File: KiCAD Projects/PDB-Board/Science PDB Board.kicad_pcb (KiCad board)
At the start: 2 copper layers, 85.1 x 63.5 mm, 12 parts, among them P1 MOTOR_PWR_OUT, P2 MAIN_PWR_IN, P3 5V_OUT, P4 PWR_REG

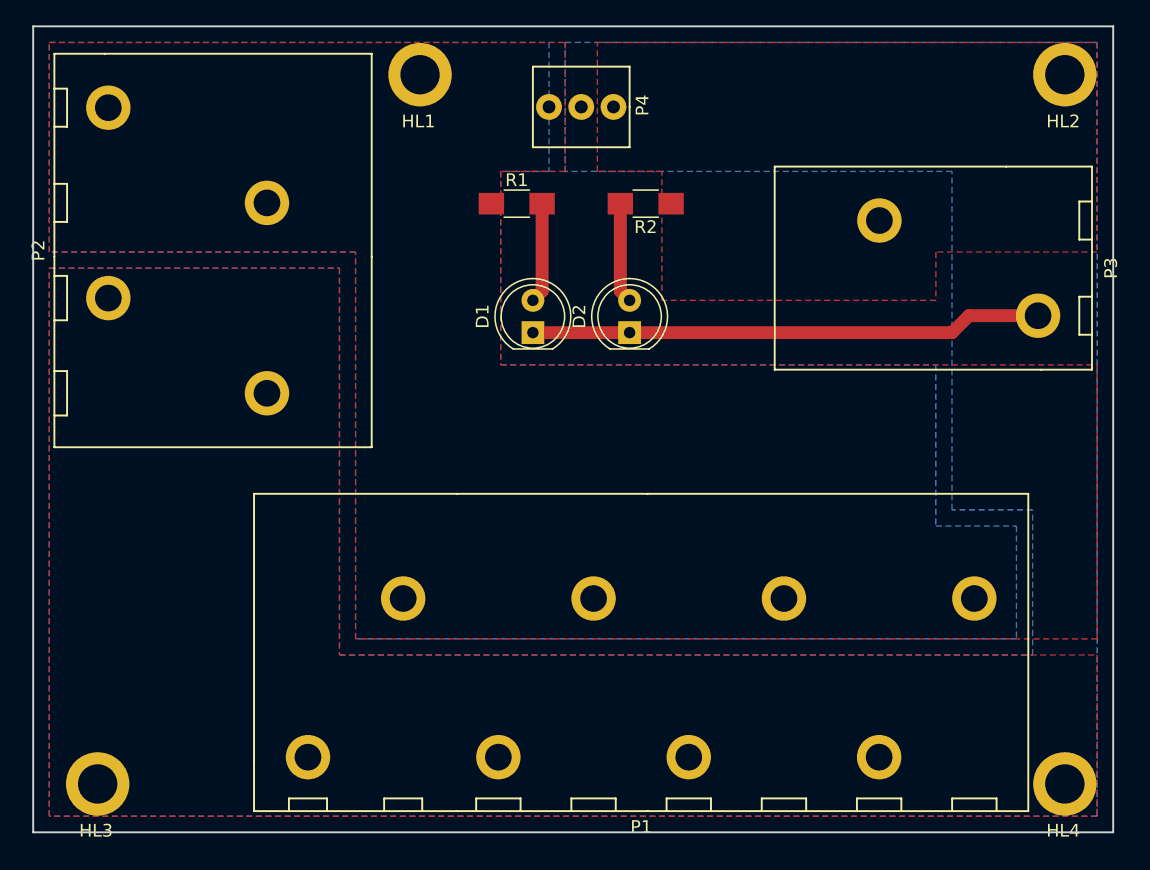
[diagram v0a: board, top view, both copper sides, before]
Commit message: Finished PDB. Actually.
Sending for review.
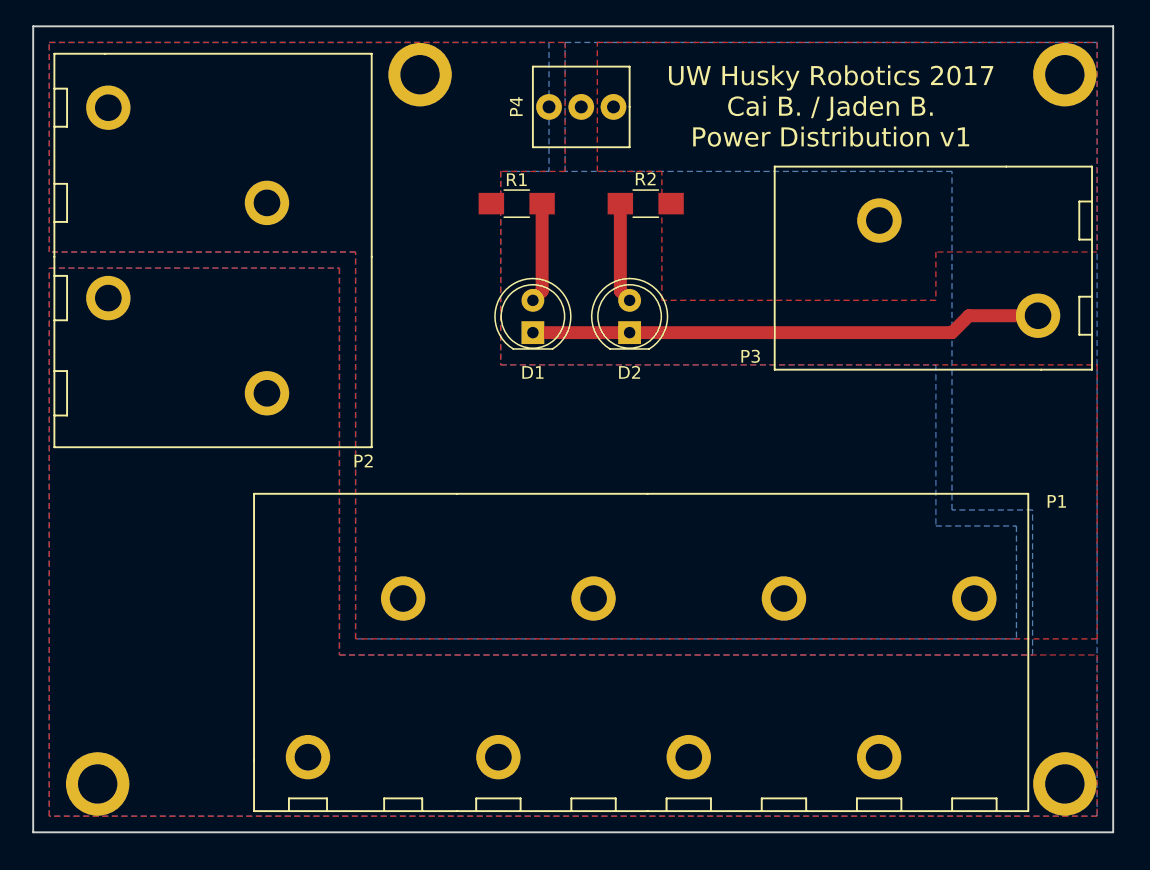
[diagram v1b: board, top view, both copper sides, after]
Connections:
- HL1 pad 1: GND -> Net-(HL1-Pad1)
- HL2 pad 1: GND -> Net-(HL2-Pad1)
- HL3 pad 1: GND -> Net-(HL3-Pad1)
- HL4 pad 1: GND -> Net-(HL4-Pad1)
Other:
- board text added: "UW Husky Robotics 2017 Cai B. / Jaden B. Power Distribution v1"
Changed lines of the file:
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@@
 (kicad_pcb (version 4) (host pcbnew 4.0.3-stable)
   (general
-    (links 24)
-    (no_connects 1)
+    (links 20)
+    (no_connects 0)
     (area 114.224999 76.124999 199.465001 139.775001)
     (thickness 1.6)
-    (drawings 4)
+    (drawings 5)
     (tracks 8)
     (zones 0)
     (modules 12)
-    (nets 6)
+    (nets 10)
   )
   (page A4)
@@
   (net 4 "Net-(D2-Pad2)")
   (net 5 GND)
+  (net 6 "Net-(HL1-Pad1)")
+  (net 7 "Net-(HL2-Pad1)")
+  (net 8 "Net-(HL3-Pad1)")
+  (net 9 "Net-(HL4-Pad1)")
   (net_class Default "This is the default net class."
     (clearance 0.2)
@@
     (add_net "Net-(D1-Pad2)")
     (add_net "Net-(D2-Pad2)")
+    (add_net "Net-(HL1-Pad1)")
+    (add_net "Net-(HL2-Pad1)")
+    (add_net "Net-(HL3-Pad1)")
+    (add_net "Net-(HL4-Pad1)")
   )
   (module Resistors_SMD:R_1206_HandSoldering (layer F.Cu)
@@
       (effects (font (size 1 1) (thickness 0.15)))
     )
-    (fp_text value R (at 0 1.9) (layer F.Fab)
+    (fp_text value R (at 0 0) (layer F.Fab)
       (effects (font (size 1 1) (thickness 0.15)))
     )
@@
     (tags "resistor 1206")
     (attr smd)
-    (fp_text reference R2 (at 0 -1.85 180) (layer F.SilkS)
-      (effects (font (size 1 1) (thickness 0.15)))
-    )
-    (fp_text value R (at 0 1.9 180) (layer F.Fab)
-      (effects (font (size 1 1) (thickness 0.15)))
-    )
-    (fp_text user %R (at 0 -1.85 180) (layer F.Fab)
+    (fp_text reference R2 (at 0 1.905 360) (layer F.SilkS)
+      (effects (font (size 1 1) (thickness 0.15)))
+    )
+    (fp_text value R (at 0 0 180) (layer F.Fab)
+      (effects (font (size 1 1) (thickness 0.15)))
+    )
+    (fp_text user %R (at 0 1.905 180) (layer F.Fab)
       (effects (font (size 1 1) (thickness 0.15)))
     )
@@
   (module .pretty:PHOENIX_1792229 (layer F.Cu)
     (at 172.72 95.25 90)
-    (fp_text reference P3 (at 0 26.5 90) (layer F.SilkS)
+    (fp_text reference P3 (at -6.985 -1.905 180) (layer F.SilkS)
       (effects (font (size 1 1) (thickness 0.15)))
     )
@@
   (module .pretty:PHOENIX_1792245 (layer F.Cu)
     (at 140.97 86.36 270)
-    (fp_text reference P2 (at 7.5 26.25 270) (layer F.SilkS)
+    (fp_text reference P2 (at 24.13 0.635 360) (layer F.SilkS)
       (effects (font (size 1 1) (thickness 0.15)))
     )
@@
   (module .pretty:PHOENIX_1792287 (layer F.Cu)
     (at 139.7 113.03)
-    (fp_text reference P1 (at 22.5 26.25) (layer F.SilkS)
+    (fp_text reference P1 (at 55.245 0.635) (layer F.SilkS)
       (effects (font (size 1 1) (thickness 0.15)))
     )
@@
   (module .pretty:MOLEX_0022232031 (layer F.Cu)
     (at 157.48 82.55)
-    (fp_text reference P4 (at 4.826 -0.127 90) (layer F.SilkS)
+    (fp_text reference P4 (at -5.08 0 270) (layer F.SilkS)
       (effects (font (size 1 1) (thickness 0.15)))
     )
@@
     (descr "LED, diameter 5.0mm, 2 pins, http://cdn-reichelt.de/documents/datenblatt/A500/LL-504BC2E-009.pdf")
     (tags "LED diameter 5.0mm 2 pins")
-    (fp_text reference D1 (at 1.27 -3.96 90) (layer F.SilkS)
+    (fp_text reference D1 (at -3.175 0 180) (layer F.SilkS)
       (effects (font (size 1 1) (thickness 0.15)))
     )
@@
     (descr "LED, diameter 5.0mm, 2 pins, http://cdn-reichelt.de/documents/datenblatt/A500/LL-504BC2E-009.pdf")
     (tags "LED diameter 5.0mm 2 pins")
-    (fp_text reference D2 (at 1.27 -3.96 90) (layer F.SilkS)
+    (fp_text reference D2 (at -3.175 0 180) (layer F.SilkS)
       (effects (font (size 1 1) (thickness 0.15)))
     )
@@
   (module hole:HOLE_M3 (layer F.Cu)
     (at 144.78 80.01)
-    (fp_text reference HL1 (at -0.127 3.683) (layer F.SilkS)
+    (fp_text reference HL1 (at -0.127 3.683) (layer F.SilkS) hide
       (effects (font (size 1 1) (thickness 0.15)))
     )
@@
     )
     (pad 1 thru_hole circle (at 0 0) (size 5 5) (drill 3.1) (layers *.Cu *.Mask)
-      (net 5 GND))
+      (net 6 "Net-(HL1-Pad1)"))
   )
   (module hole:HOLE_M3 (layer F.Cu)
     (at 195.58 80.01)
-    (fp_text reference HL2 (at -0.127 3.683) (layer F.SilkS)
+    (fp_text reference HL2 (at -0.127 3.683) (layer F.SilkS) hide
       (effects (font (size 1 1) (thickness 0.15)))
     )
@@
     )
     (pad 1 thru_hole circle (at 0 0) (size 5 5) (drill 3.1) (layers *.Cu *.Mask)
-      (net 5 GND))
+      (net 7 "Net-(HL2-Pad1)"))
   )
   (module hole:HOLE_M3 (layer F.Cu)
     (at 119.38 135.89)
-    (fp_text reference HL3 (at -0.127 3.683) (layer F.SilkS)
+    (fp_text reference HL3 (at -0.127 3.683) (layer F.SilkS) hide
       (effects (font (size 1 1) (thickness 0.15)))
     )
@@
     )
     (pad 1 thru_hole circle (at 0 0) (size 5 5) (drill 3.1) (layers *.Cu *.Mask)
-      (net 5 GND))
+      (net 8 "Net-(HL3-Pad1)"))
   )
   (module hole:HOLE_M3 (layer F.Cu)
     (at 195.58 135.89)
-    (fp_text reference HL4 (at -0.127 3.683) (layer F.SilkS)
+    (fp_text reference HL4 (at -0.127 3.683) (layer F.SilkS) hide
       (effects (font (size 1 1) (thickness 0.15)))
     )
@@
     )
     (pad 1 thru_hole circle (at 0 0) (size 5 5) (drill 3.1) (layers *.Cu *.Mask)
-      (net 5 GND))
+      (net 9 "Net-(HL4-Pad1)"))
+  )
+  (gr_text "UW Husky Robotics 2017\nCai B. / Jaden B.\nPower Distribution v1" (at 177.165 82.55) (layer F.SilkS)
+    (effects (font (size 1.5 1.5) (thickness 0.3)))
   )
   (gr_line (start 114.3 139.7) (end 114.3 76.2) (angle 90) (layer Edge.Cuts) (width 0.15))
@@
       )
     )
+  )
+  (zone (net 0) (net_name "") (layer B.Mask) (hatch edge 0.508)
+    (connect_pads (clearance 0.508))
+    (min_thickness 0.254)
+    (fill yes (arc_segments 16) (thermal_gap 0.508) (thermal_bridge_width 0.508))
+    (polygon
+      (pts
+        (xy 128.905 109.22) (xy 137.795 109.22) (xy 137.795 126.365) (xy 193.04 126.365) (xy 193.04 130.175)
+        (xy 132.08 130.175) (xy 132.08 136.525) (xy 124.46 136.525) (xy 124.46 130.81) (xy 117.475 130.81)
+        (xy 117.475 101.6) (xy 128.905 101.6)
+      )
+    )
+  )
+  (zone (net 0) (net_name "") (layer B.Mask) (hatch edge 0.508)
+    (connect_pads (clearance 0.508))
+    (min_thickness 0.254)
+    (fill yes (arc_segments 16) (thermal_gap 0.508) (thermal_bridge_width 0.508))
+    (polygon
+      (pts
+        (xy 139.7 84.455) (xy 150.495 84.455) (xy 150.495 103.505) (xy 184.785 103.505) (xy 184.785 117.475)
+        (xy 140.335 117.475) (xy 140.335 93.345) (xy 136.525 93.345) (xy 136.525 86.36) (xy 123.825 86.36)
+        (xy 123.825 78.105) (xy 139.7 78.105)
+      )
+    )
+  )
+  (zone (net 0) (net_name "") (layer F.Mask) (hatch edge 0.508)
+    (connect_pads (clearance 0.508))
+    (min_thickness 0.254)
+    (fill yes (arc_segments 16) (thermal_gap 0.508) (thermal_bridge_width 0.508))
+    (polygon
+      (pts
+        (xy 129.54 130.81) (xy 117.475 130.81) (xy 117.475 111.76) (xy 129.54 111.76)
+      )
+    )
+  )
+  (zone (net 0) (net_name "") (layer F.Mask) (hatch edge 0.508)
+    (connect_pads (clearance 0.508))
+    (min_thickness 0.254)
+    (fill yes (arc_segments 16) (thermal_gap 0.508) (thermal_bridge_width 0.508))
+    (polygon
+      (pts
+        (xy 150.495 104.775) (xy 196.215 104.775) (xy 196.215 111.125) (xy 142.875 111.125) (xy 142.875 93.98)
+        (xy 150.495 93.98)
+      )
+    )

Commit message: Worked on PDB
Added silkscreen and silkscreen cutout segmentation as per feedback from
Justin.
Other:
- board text added: "+"
- board text added: "+12Vi"
- board text added: "+5Vo"
- board text added: "-"
- board text added: "GND"
- board text added: "M1+"
- board text added: "M1-"
- board text added: "M2+"
- board text added: "M2-"
- board text added: "M3+"
- board text added: "M3-"
- board text added: "M4+"
- board text added: "M4-"
- board text added: "UW Husky Robotics 2017 Cai B. / Jaden B. Sci Power Distribution v1"
- board text removed: "UW Husky Robotics 2017 Cai B. / Jaden B. Power Distribution v1"
